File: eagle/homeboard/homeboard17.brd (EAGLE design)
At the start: 100 x 80 mm, 126 parts, among them IC1 XCF02S, IC2 25LC080SN, IC3 ATMEGA32U2-TQFP, Q5 BC848SMD, Q6 BC848SMD, Q7 BC848SMD, Q8 BC848SMD, T1 BSS138, T2 BC848, T3 BSS138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

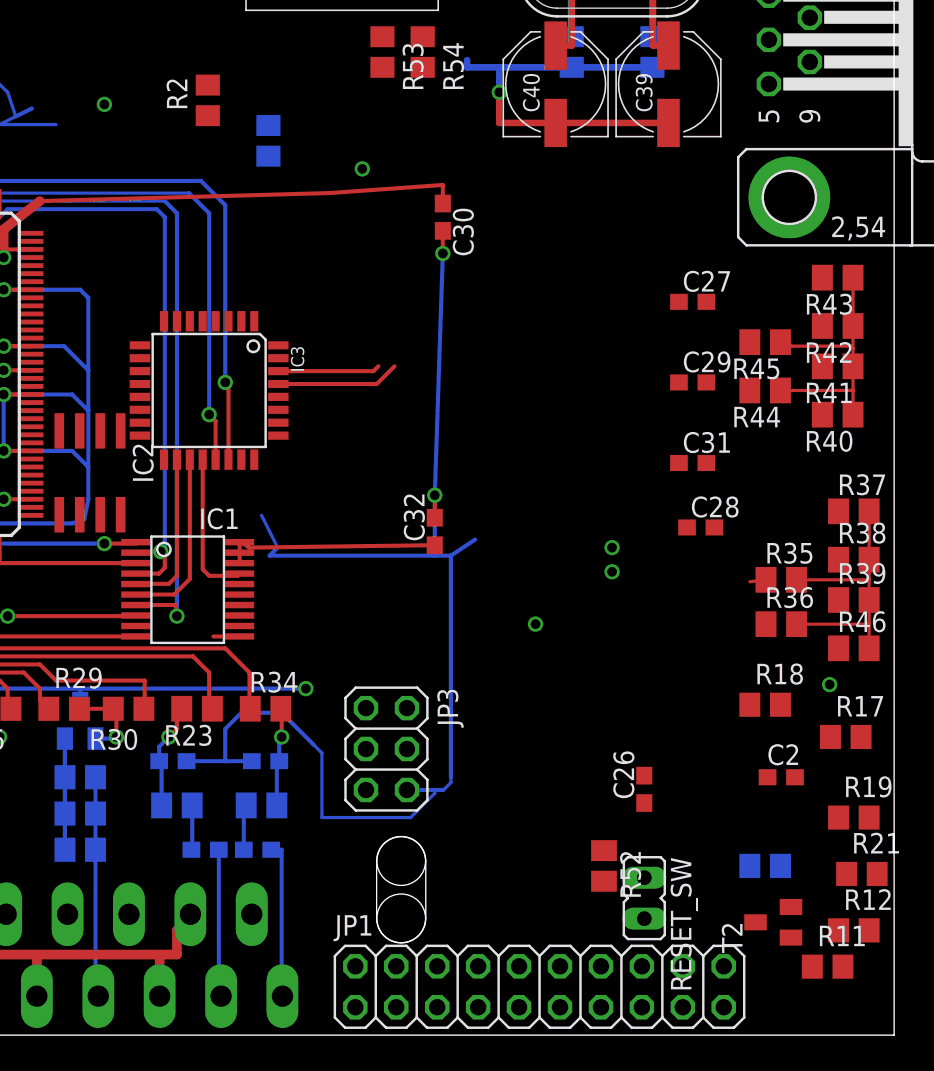
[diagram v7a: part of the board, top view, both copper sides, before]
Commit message: removing dead vias
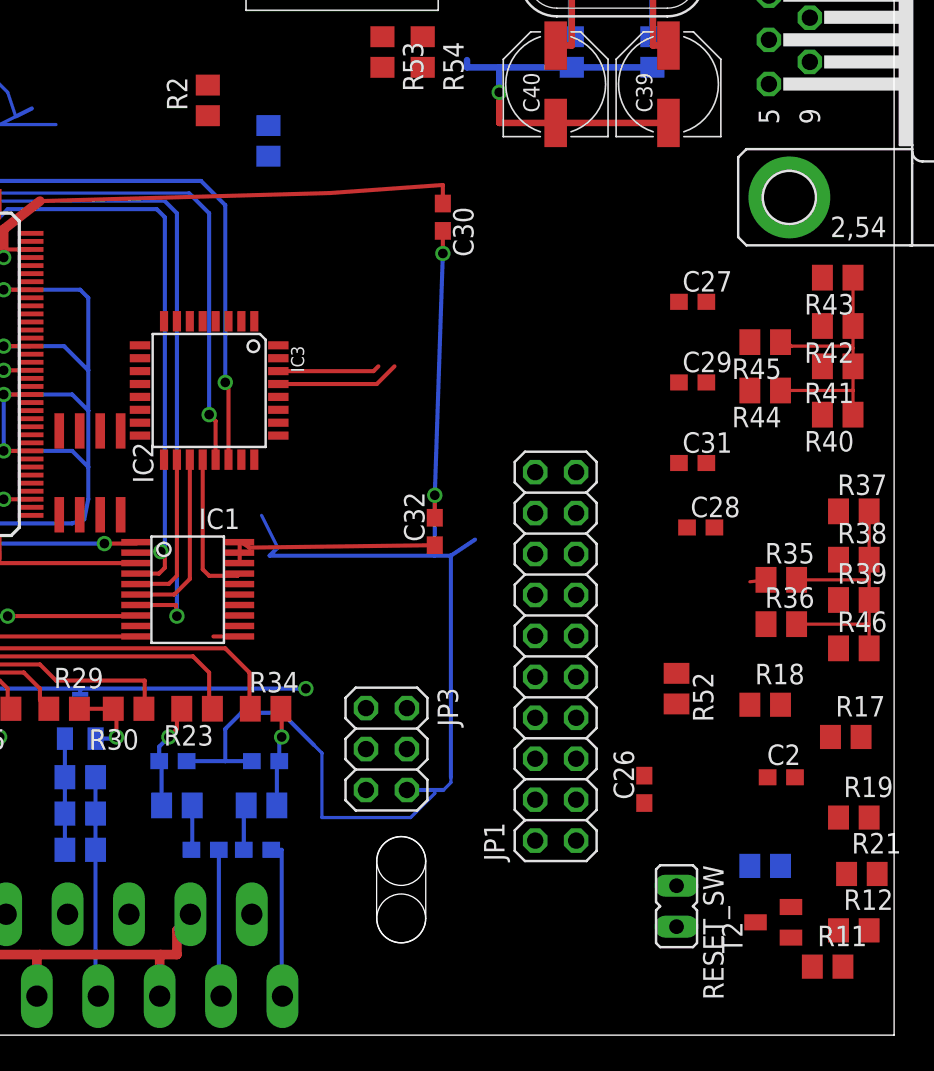
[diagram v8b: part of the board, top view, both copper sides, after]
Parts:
- moved JP1 20.5 mm to (79.0, 23.5), turned to 90 degrees
- moved R52 11.9 mm to (86.5, 21.5)
- moved RESET_SW 2.06 mm to (86.5, 8.00)
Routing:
- net GND: vias 34 -> 28
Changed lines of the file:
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@@
 <element name="R49" library="resistor" package="M0805" value="" x="60.75" y="14.25" rot="MR0"/>
 <element name="R50" library="resistor" package="M0805" value="2k2" x="21.25" y="19.25" rot="R180"/>
-<element name="RESET_SW" library="jumper" package="JP1" value="" x="84.5" y="8.5" rot="R180"/>
-<element name="R52" library="resistor" package="M0805" value="4K7" x="82" y="10.5" rot="R270"/>
+<element name="RESET_SW" library="jumper" package="JP1" value="" x="86.5" y="8" rot="R180"/>
+<element name="R52" library="resistor" package="M0805" value="4K7" x="86.5" y="21.5" rot="R270"/>
 <element name="IC3" library="adafruit" package="TQFP32-08" value="ATMEGA32U2-TQFP" x="57.5" y="40" rot="R270"/>
 <element name="U$4" library="cpcfpga" package="SOT223" value="3.3V" x="8.5" y="34" rot="R270"/>
@@
 <element name="C35" library="rcl" package="PANASONIC_D" value="100u" x="6" y="29" rot="MR0"/>
 <element name="C36" library="rcl" package="PANASONIC_D" value="100u" x="6" y="20" rot="R180"/>
-<element name="JP1" library="pinhead" package="2X10" value="" x="78" y="3"/>
+<element name="JP1" library="pinhead" package="2X10" value="" x="79" y="23.5" rot="R90"/>
 <element name="X7" library="powersupply" package="DC-21MM" value="DC21MMX" x="4" y="7" rot="R180"/>
 <element name="SV3" library="con-lstb" package="MA10-1" value="" x="24" y="59">
@@
 <wire x1="29.5" y1="7.5" x2="29.665" y2="7.5" width="0.254" layer="1"/>
 <wire x1="20" y1="13.75" x2="20" y2="3" width="0.254" layer="16"/>
-<via x="82.5" y="30.25" extent="1-16" drill="0.6" shape="square"/>
-<via x="82.5" y="28.75" extent="1-16" drill="0.6" shape="square"/>
 <wire x1="20" y1="3" x2="23.37" y2="3" width="0.254" layer="16"/>
 <wire x1="23.37" y1="3" x2="23.95" y2="2.42" width="0.254" layer="16"/>
-<via x="96" y="21.75" extent="1-16" drill="0.6" shape="square"/>
 <wire x1="49" y1="31.75" x2="49.75" y2="32" width="0.254" layer="16"/>
 <wire x1="59.393396875" y1="24.737409375" x2="57.762590625" y2="24.737409375" width="0.254" layer="1"/>
-<via x="77.75" y="25.5" extent="1-16" drill="0.6" shape="square"/>
 <contactref element="JP3" pad="6"/>
 <wire x1="69.77" y1="15.21" x2="71.5" y2="15.21" width="0.254" layer="16"/>
@@
 <wire x1="25.02" y1="39.25" x2="28.5" y2="39.25" width="0.254" layer="1"/>
 <via x="28.5" y="39.25" extent="1-16" drill="0.6" shape="square"/>
-<via x="67" y="53.75" extent="1-16" drill="0.6" shape="square"/>
 <wire x1="30.97" y1="30.3" x2="30.97" y2="31.72" width="0.254" layer="1"/>
 <wire x1="30.97" y1="31.72" x2="30.75" y2="31.75" width="0.254" layer="1"/>
@@
 <contactref element="U$6" pad="P24"/>
 <wire x1="18.25" y1="31" x2="18.25" y2="30" width="0.254" layer="1"/>
-<via x="51" y="57.75" extent="1-16" drill="0.6" shape="square"/>
 <contactref element="U$6" pad="P30"/>
 <wire x1="21.25" y1="31" x2="21.25" y2="30" width="0.254" layer="1"/>
@@
 <wire x1="72" y1="49.9" x2="75.5" y2="56.6" width="0" layer="19" extent="1-1"/>
 <wire x1="59.393396875" y1="24.737409375" x2="59.5" y2="20" width="0" layer="19" extent="1-16"/>
-<wire x1="67" y1="53.75" x2="72" y2="49.9" width="0" layer="19" extent="1-1"/>
-<wire x1="77.75" y1="25.5" x2="74" y2="30.75" width="0" layer="19" extent="16-16"/>
-<wire x1="82.5" y1="28.75" x2="77.75" y2="25.5" width="0" layer="19" extent="1-1"/>
-<wire x1="82.5" y1="30.25" x2="82.5" y2="28.75" width="0" layer="19" extent="1-1"/>
-<wire x1="88.85" y1="31.5" x2="82.5" y2="30.25" width="0" layer="19" extent="1-1"/>
-<wire x1="88.35" y1="35.5" x2="88.85" y2="31.5" width="0" layer="19" extent="1-1"/>
-<wire x1="88.35" y1="40.5" x2="88.35" y2="35.5" width="0" layer="19" extent="1-1"/>
-<wire x1="88.35" y1="45.5" x2="88.35" y2="40.5" width="0" layer="19" extent="1-1"/>
 <wire x1="56.5" y1="8.5" x2="56.1" y2="17" width="0" layer="19" extent="1-16"/>
 <wire x1="15" y1="59" x2="15.11" y2="59" width="0" layer="19" extent="16-16"/>
@@
 <wire x1="29.47" y1="51.7" x2="29.5" y2="51.75" width="0" layer="19" extent="1-1"/>
 <wire x1="48.198553125" y1="37.4890875" x2="49" y2="36.25" width="0" layer="19" extent="1-16"/>
-<wire x1="51" y1="57.75" x2="48" y2="56.5" width="0" layer="19" extent="16-16"/>
 <wire x1="19.2" y1="66.75" x2="24" y2="64" width="0" layer="19" extent="16-16"/>
 <wire x1="29.9778" y1="68.25" x2="27.5" y2="62" width="0" layer="19" extent="16-16"/>
 <wire x1="43.8716" y1="69.52" x2="41.5" y2="62" width="0" layer="19" extent="16-16"/>
+<wire x1="80.27" y1="12.07" x2="72.5" y2="15.67" width="0" layer="19" extent="16-16"/>
+<wire x1="84.5" y1="16.1" x2="80.27" y2="12.07" width="0" layer="19" extent="1-1"/>
+<wire x1="86.5" y1="6.73" x2="80.27" y2="12.07" width="0" layer="19" extent="1-1"/>
 <wire x1="58.7" y1="44.2926" x2="50" y2="45.75" width="0" layer="19" extent="1-16"/>
-<wire x1="66.57" y1="1.73" x2="55.5" y2="5" width="0" layer="19" extent="1-1"/>
-<wire x1="84.5" y1="16.1" x2="77.75" y2="25.5" width="0" layer="19" extent="1-1"/>
-<wire x1="84.5" y1="7.23" x2="84.5" y2="16.1" width="0" layer="19" extent="1-1"/>
-<wire x1="96.05" y1="18.5" x2="84.5" y2="16.1" width="0" layer="19" extent="1-1"/>
-<wire x1="96" y1="21.75" x2="96.05" y2="18.5" width="0" layer="19" extent="1-1"/>
-<wire x1="96.55" y1="13.5" x2="96.05" y2="18.5" width="0" layer="19" extent="1-1"/>
-<wire x1="97.05" y1="10" x2="96.55" y2="13.5" width="0" layer="19" extent="1-1"/>
-<wire x1="96.55" y1="6.5" x2="97.05" y2="10" width="0" layer="19" extent="1-1"/>
+<wire x1="96.55" y1="6.5" x2="86.5" y2="6.73" width="0" layer="19" extent="1-1"/>
+<wire x1="97.05" y1="10" x2="96.55" y2="6.5" width="0" layer="19" extent="1-1"/>
+<wire x1="96.55" y1="13.5" x2="97.05" y2="10" width="0" layer="19" extent="1-1"/>
+<wire x1="96.05" y1="18.5" x2="96.55" y2="13.5" width="0" layer="19" extent="1-1"/>
+<wire x1="88.35" y1="45.5" x2="86" y2="56.5" width="0" layer="19" extent="1-1"/>
+<wire x1="88.35" y1="40.5" x2="88.35" y2="45.5" width="0" layer="19" extent="1-1"/>
+<wire x1="88.35" y1="35.5" x2="88.35" y2="40.5" width="0" layer="19" extent="1-1"/>
+<wire x1="88.85" y1="31.5" x2="88.35" y2="35.5" width="0" layer="19" extent="1-1"/>
 </signal>
 <signal name="VCC">
@@
 <wire x1="86.65" y1="35.5" x2="86.65" y2="40.5" width="0" layer="19" extent="1-1"/>
 <wire x1="87.15" y1="31.5" x2="86.65" y2="35.5" width="0" layer="19" extent="1-1"/>
-<wire x1="92.95" y1="10.5" x2="98.45" y2="24" width="0" layer="19" extent="1-16"/>
+<wire x1="86.5" y1="22.45" x2="93.95" y2="25.5" width="0" layer="19" extent="1-1"/>
+<wire x1="84.5" y1="14.4" x2="86.5" y2="22.45" width="0" layer="19" extent="1-1"/>
+<wire x1="77.73" y1="12.07" x2="84.5" y2="14.4" width="0" layer="19" extent="1-1"/>
+<wire x1="92.95" y1="10.5" x2="84.5" y2="14.4" width="0" layer="19" extent="1-16"/>
 <wire x1="91.4" y1="7" x2="92.95" y2="10.5" width="0" layer="19" extent="1-16"/>
-<wire x1="84.5" y1="14.4" x2="92.95" y2="10.5" width="0" layer="19" extent="1-16"/>
-<wire x1="82" y1="11.45" x2="84.5" y2="14.4" width="0" layer="19" extent="1-1"/>
-<wire x1="69.77" y1="17.75" x2="82" y2="11.45" width="0" layer="19" extent="1-1"/>
+<wire x1="69.77" y1="17.75" x2="77.73" y2="12.07" width="0" layer="19" extent="1-1"/>
 <wire x1="63.5" y1="21.5" x2="69.77" y2="17.75" width="0" layer="19" extent="1-1"/>
 <wire x1="12.57" y1="24.5" x2="12.5" y2="24.47" width="0" layer="19" extent="1-1"/>
@@
 <wire x1="61.7926" y1="42" x2="61.7926" y2="42.8" width="0" layer="19" extent="1-1"/>
 <wire x1="57.9" y1="44.2926" x2="61.7926" y2="42.8" width="0" layer="19" extent="1-1"/>
-<wire x1="66.57" y1="4.27" x2="69.77" y2="17.75" width="0" layer="19" extent="1-1"/>
 </signal>
 <signal name="TCK">
@@
 <contactref element="X4" pad="4"/>
 <contactref element="R43" pad="2"/>
-<wire x1="95.2432" y1="46.7432" x2="95.5" y2="47" width="0.2" layer="1"/>
-<wire x1="95.5" y1="47" x2="95.55" y2="47" width="0" layer="19" extent="1-1"/>
-<wire x1="45.2432" y1="66.98" x2="95.2432" y2="46.7432" width="0" layer="19" extent="1-1"/>
+<wire x1="45.2432" y1="66.98" x2="95.55" y2="47" width="0" layer="19" extent="1-1"/>
 </signal>
 <signal name="N$47">
@@
 <contactref element="R52" pad="2"/>
 <contactref element="RESET_SW" pad="1"/>
-<wire x1="82" y1="9.55" x2="84.5" y2="9.77" width="0" layer="19" extent="1-1"/>
+<wire x1="86.5" y1="9.27" x2="86.5" y2="20.55" width="0" layer="19" extent="1-1"/>
 </signal>
 <signal name="CLK16">
@@
 <wire x1="80" y1="61.95" x2="79.96" y2="61.95" width="0.4064" layer="16"/>
 <wire x1="79.96" y1="61.95" x2="79.96" y2="65.5" width="0.4064" layer="16"/>
-<wire x1="80" y1="65.5" x2="80" y2="69.238" width="0" layer="19" extent="1-16"/>
 <wire x1="80" y1="69.238" x2="79.96" y2="69.238" width="0.4064" layer="1"/>
 <wire x1="79.96" y1="69.238" x2="79.96" y2="65.5" width="0.4064" layer="1"/>
 <wire x1="79" y1="61.4" x2="80" y2="61.4" width="0.4064" layer="1"/>
 <wire x1="80" y1="61.4" x2="80" y2="65.5" width="0.4064" layer="1"/>
+<wire x1="80" y1="65.5" x2="79.96" y2="65.5" width="0" layer="19" extent="1-1"/>
 </signal>
 <signal name="N$14">
